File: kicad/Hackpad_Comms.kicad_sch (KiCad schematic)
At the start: 26 parts, among them SW1 SW_Push, SW10 SW_Push, SW11 SW_Push, SW12 SW_Push, SW14 RotaryEncoder, SW2 SW_Push, SW3 SW_Push, SW4 SW_Push, SW5 SW_Push, SW6 SW_Push, SW7 SW_Push, SW8 SW_Push, SW9 SW_Push, U1 XIAO-RP2040-DIP

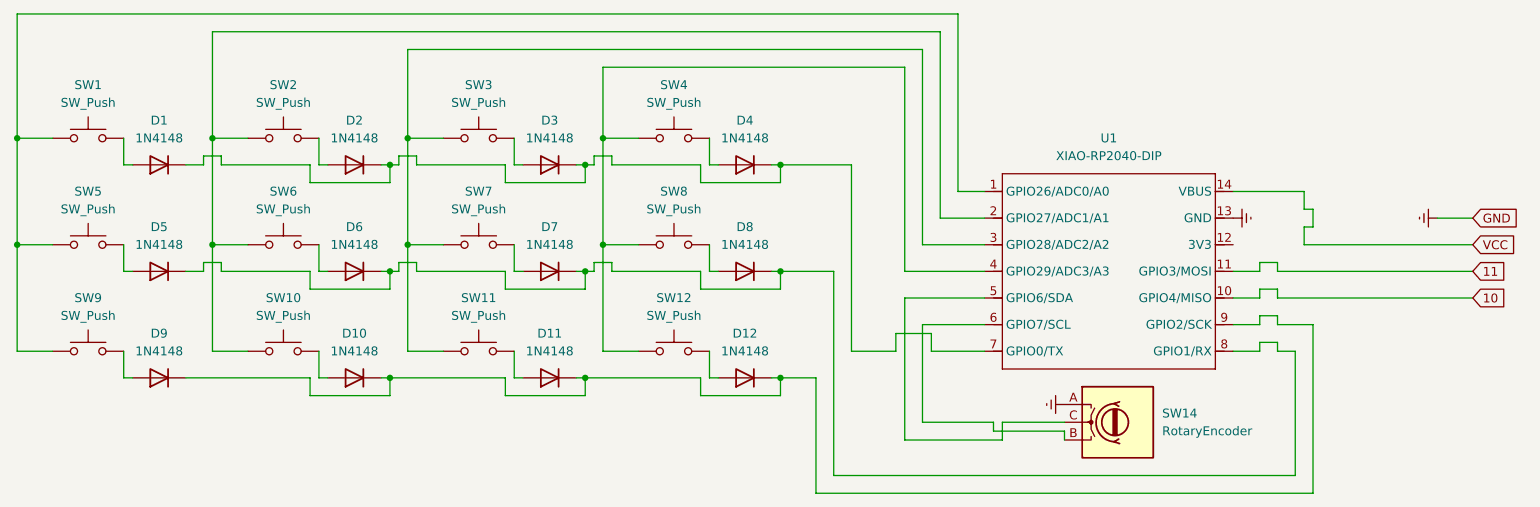
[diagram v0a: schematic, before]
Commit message: PCB Rev2; Add more images; Basic HID firmware prototype
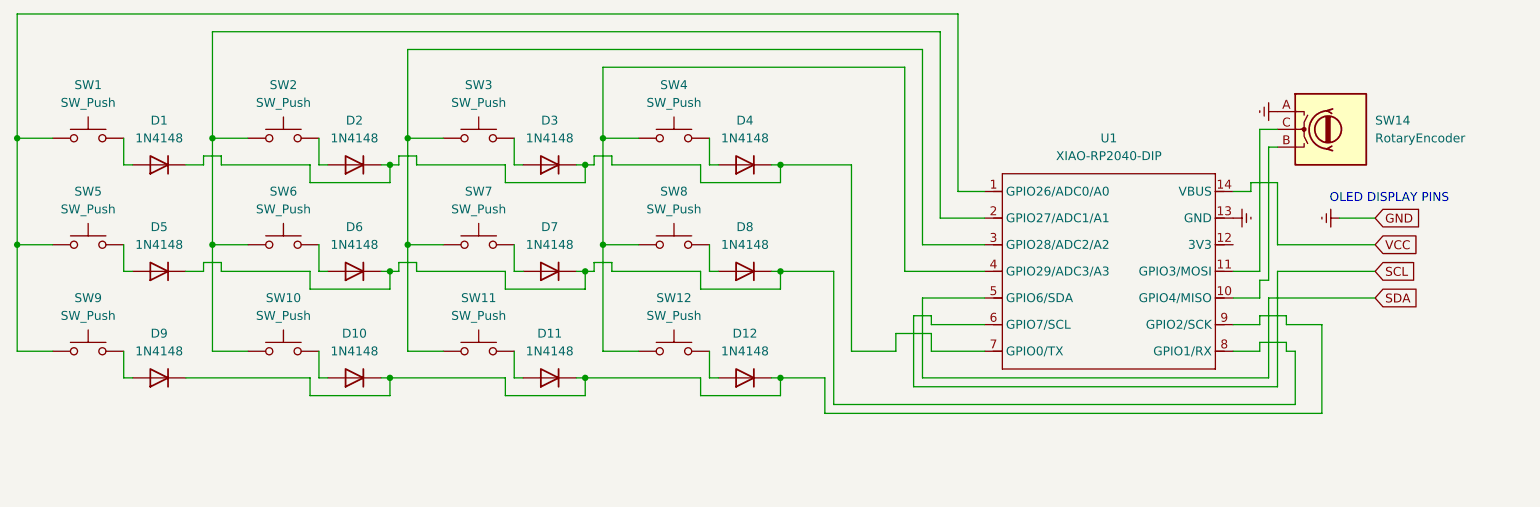
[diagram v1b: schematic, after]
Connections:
- net 10 is gone; now on an unnamed net: U1.10 (GPIO4/MISO)
- net 11 is gone; now on an unnamed net: U1.11 (GPIO3/MOSI)
- net at SW14.B: no longer U1.6 (GPIO7/SCL)
- net at SW14.C: no longer U1.5 (GPIO6/SDA)
- new net SCL: U1.6 (GPIO7/SCL)
- new net SDA: U1.5 (GPIO6/SDA)
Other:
- note added: "OLED DISPLAY PINS"
- moved on the sheet: SW14
